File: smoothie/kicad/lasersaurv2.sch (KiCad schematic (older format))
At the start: 25 parts, among them IC1 74LV11, IC2 74HCT08, J1 DOOR1, J2 DOOR2, J3 CHILLER, J4 TO_J8, J6 TO_AUX1, J7 LASER_AUX, J8 LASER

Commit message: Fix bug where door inputs were connected before the filter.
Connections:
- net P2.11: now also C2.1, IC1.5 (2C), R7.1; no longer J2.2 (P2), R4.2, R7.2
- net P2.12: now also C3.1, IC1.4 (2B), R6.1; no longer J1.2 (P2), R3.2, R6.2
- net P4.28: now also C1.1, IC1.2 (1B), R8.1; no longer J3.2 (P2), R5.2, R8.2
- new net: J1.2 (P2), R3.2, R6.2
- new net: J2.2 (P2), R4.2, R7.2
- new net: J3.2 (P2), R5.2, R8.2
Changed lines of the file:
@@
 	1    0    0    -1
 $EndComp
-Text GLabel 3000 4250 1    60   Input ~ 0
+Text GLabel 4050 4300 1    60   Input ~ 0
 P2.11
-Text GLabel 3150 4250 1    60   Input ~ 0
+Text GLabel 4250 4300 1    60   Input ~ 0
 P2.12
-Text GLabel 3600 2700 1    60   Input ~ 0
+Text GLabel 4100 2700 1    60   Input ~ 0
 P4.28
 $Comp
@@
 Wire Wire Line
 	2650 4650 3650 4650
-Connection ~ 3000 4650
-Connection ~ 3150 4550
 Wire Wire Line
 	4950 3450 5500 3450
@@
 Wire Wire Line
 	3150 2950 3700 2950
-Wire Wire Line
-	3600 2900 3600 3000
 Connection ~ 3600 2950
 $Comp
@@
 	2400 5350 2400 5150
 Wire Wire Line
-	3150 4250 3150 4550
-Wire Wire Line
-	3000 4250 3000 4650
-Wire Wire Line
 	2650 5350 2650 4650
 Connection ~ 2400 5350
@@
 	3600 3300 3600 3400
 Wire Wire Line
-	3600 2950 3600 2700
-Wire Wire Line
 	3600 3350 4100 3350
 Wire Wire Line
@@
 	4950 2950 4950 3450
 Wire Wire Line
-	4100 2950 4100 3000
+	4100 2700 4100 3000
 Connection ~ 4100 2950
 $Comp
@@
 Wire Wire Line
 	2250 1150 2250 1000
+Wire Wire Line
+	3600 2950 3600 3000
+Wire Wire Line
+	4050 4300 4050 4650
+Connection ~ 4050 4650
+Wire Wire Line
+	4250 4300 4250 4550
+Connection ~ 4250 4550
 $EndSCHEMATC

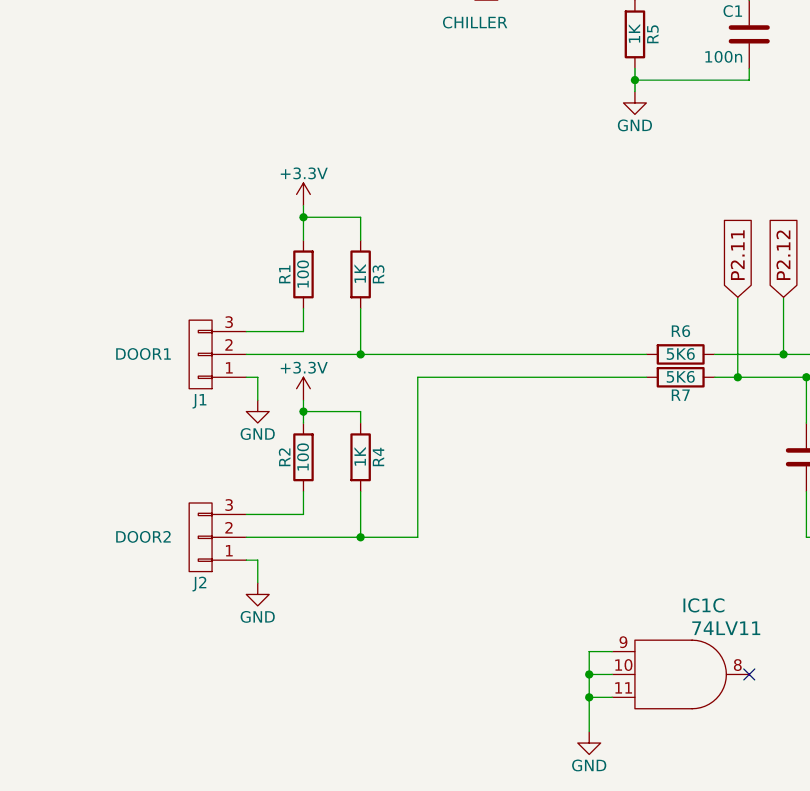
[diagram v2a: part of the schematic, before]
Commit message: Fix door switch high/low.
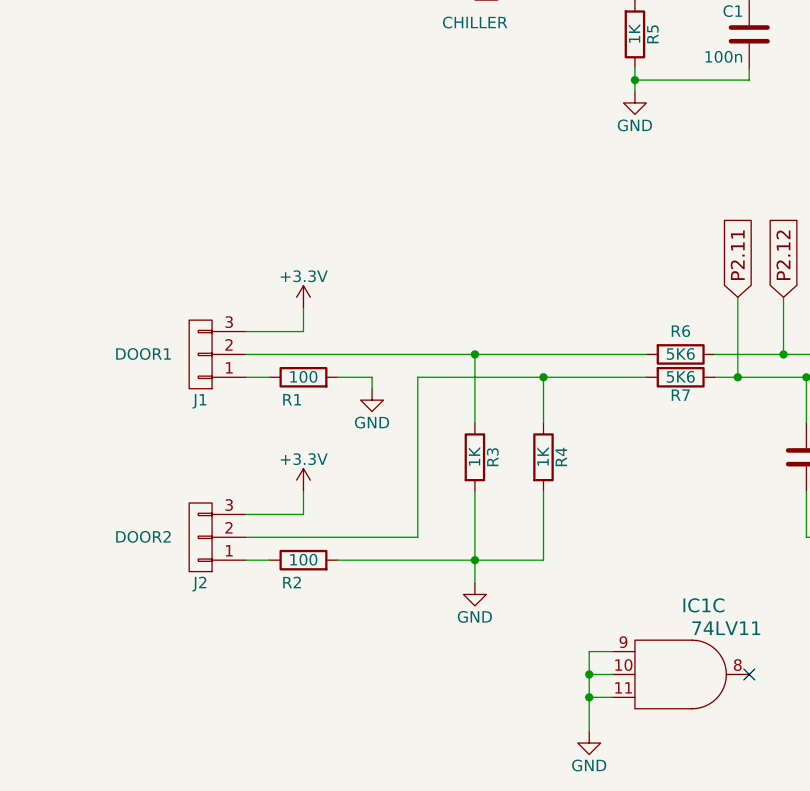
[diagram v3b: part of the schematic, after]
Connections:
- net +3V3: now also J1.3 (P3), J2.3 (P3); no longer R1.2, R2.2, R3.1, R4.1
- net GND: now also R1.2, R2.2, R3.2, R4.2; no longer J1.1 (P1), J2.1 (P1)
- net at J1.2 (P2), R6.2: now also R3.1; no longer R3.2
- net at J2.2 (P2), R7.2: now also R4.1; no longer R4.2
- net at R1.1: now also J1.1 (P1); no longer J1.3 (P3)
- net at R2.1: now also J2.1 (P1); no longer J2.3 (P3)
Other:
- moved on the sheet: R1, R2, R3, R4
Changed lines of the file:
@@
 L R R3
 U 1 1 58F2E564
-P 2400 4200
-F 0 "R3" V 2480 4200 50  0000 C CNN
-F 1 "1K" V 2400 4200 50  0000 C CNN
-F 2 "Resistors_SMD:R_0603" V 2330 4200 50  0001 C CNN
-F 3 "" H 2400 4200 50  0000 C CNN
-	1    2400 4200
+P 2900 5000
+F 0 "R3" V 2980 5000 50  0000 C CNN
+F 1 "1K" V 2900 5000 50  0000 C CNN
+F 2 "Resistors_SMD:R_0603" V 2830 5000 50  0001 C CNN
+F 3 "" H 2900 5000 50  0000 C CNN
+	1    2900 5000
 	1    0    0    -1
 $EndComp
@@
 L R R4
 U 1 1 58F2E56B
-P 2400 5000
-F 0 "R4" V 2480 5000 50  0000 C CNN
-F 1 "1K" V 2400 5000 50  0000 C CNN
-F 2 "Resistors_SMD:R_0603" V 2330 5000 50  0001 C CNN
-F 3 "" H 2400 5000 50  0000 C CNN
-	1    2400 5000
+P 3200 5000
+F 0 "R4" V 3280 5000 50  0000 C CNN
+F 1 "1K" V 3200 5000 50  0000 C CNN
+F 2 "Resistors_SMD:R_0603" V 3130 5000 50  0001 C CNN
+F 3 "" H 3200 5000 50  0000 C CNN
+	1    3200 5000
 	1    0    0    -1
 $EndComp
@@
 L R R1
 U 1 1 58F2E6E6
-P 2150 4200
-F 0 "R1" V 2230 4200 50  0000 C CNN
-F 1 "100" V 2150 4200 50  0000 C CNN
-F 2 "Resistors_SMD:R_0603" V 2080 4200 50  0001 C CNN
-F 3 "" H 2150 4200 50  0000 C CNN
-	1    2150 4200
-	-1   0    0    1
+P 2150 4650
+F 0 "R1" V 2050 4700 50  0000 C CNN
+F 1 "100" V 2150 4650 50  0000 C CNN
+F 2 "Resistors_SMD:R_0603" V 2080 4650 50  0001 C CNN
+F 3 "" H 2150 4650 50  0000 C CNN
+	1    2150 4650
+	0    -1   -1   0
 $EndComp
 $Comp
 L GND #PWR010
 U 1 1 58F2E6ED
-P 1950 4750
-F 0 "#PWR010" H 1950 4500 50  0001 C CNN
-F 1 "GND" H 1950 4600 50  0000 C CNN
-F 2 "" H 1950 4750 50  0000 C CNN
-F 3 "" H 1950 4750 50  0000 C CNN
-	1    1950 4750
+P 2450 4700
+F 0 "#PWR010" H 2450 4450 50  0001 C CNN
+F 1 "GND" H 2450 4550 50  0000 C CNN
+F 2 "" H 2450 4700 50  0000 C CNN
+F 3 "" H 2450 4700 50  0000 C CNN
+	1    2450 4700
 	1    0    0    -1
 $EndComp
@@
 L R R2
 U 1 1 58F2E700
-P 2150 5000
-F 0 "R2" V 2230 5000 50  0000 C CNN
-F 1 "100" V 2150 5000 50  0000 C CNN
-F 2 "Resistors_SMD:R_0603" V 2080 5000 50  0001 C CNN
-F 3 "" H 2150 5000 50  0000 C CNN
-	1    2150 5000
-	-1   0    0    1
+P 2150 5450
+F 0 "R2" V 2050 5500 50  0000 C CNN
+F 1 "100" V 2150 5450 50  0000 C CNN
+F 2 "Resistors_SMD:R_0603" V 2080 5450 50  0001 C CNN
+F 3 "" H 2150 5450 50  0000 C CNN
+	1    2150 5450
+	0    -1   -1   0
 $EndComp
 $Comp
 L GND #PWR011
 U 1 1 58F2E707
-P 1950 5550
-F 0 "#PWR011" H 1950 5300 50  0001 C CNN
-F 1 "GND" H 1950 5400 50  0000 C CNN
-F 2 "" H 1950 5550 50  0000 C CNN
-F 3 "" H 1950 5550 50  0000 C CNN
-	1    1950 5550
+P 2900 5550
+F 0 "#PWR011" H 2900 5300 50  0001 C CNN
+F 1 "GND" H 2900 5400 50  0000 C CNN
+F 2 "" H 2900 5550 50  0000 C CNN
+F 3 "" H 2900 5550 50  0000 C CNN
+	1    2900 5550
 	1    0    0    -1
 $EndComp
@@
 	1900 4550 3650 4550
 Wire Wire Line
-	2400 4550 2400 4350
-Connection ~ 2400 4550
-Wire Wire Line
-	1900 4650 1950 4650
-Wire Wire Line
-	1950 4650 1950 4750
+	1900 4650 2000 4650
 Wire Wire Line
 	2150 5150 2150 5250
@@
 	1900 5350 2650 5350
 Wire Wire Line
-	2400 5350 2400 5150
-Wire Wire Line
 	2650 5350 2650 4650
-Connection ~ 2400 5350
-Wire Wire Line
-	1900 5450 1950 5450
-Wire Wire Line
-	1950 5450 1950 5550
 $Comp
 L +3.3V #PWR016
 U 1 1 58F316F9
-P 2150 3900
-F 0 "#PWR016" H 2150 3750 50  0001 C CNN
-F 1 "+3.3V" H 2150 4040 50  0000 C CNN
-F 2 "" H 2150 3900 50  0001 C CNN
-F 3 "" H 2150 3900 50  0001 C CNN
-	1    2150 3900
-	1    0    0    -1
-$EndComp
-Wire Wire Line
-	2150 3900 2150 4050
-Wire Wire Line
-	2400 4050 2400 3950
-Wire Wire Line
-	2400 3950 2150 3950
-Connection ~ 2150 3950
+P 2150 4350
+F 0 "#PWR016" H 2150 4200 50  0001 C CNN
+F 1 "+3.3V" H 2150 4490 50  0000 C CNN
+F 2 "" H 2150 4350 50  0001 C CNN
+F 3 "" H 2150 4350 50  0001 C CNN
+	1    2150 4350
+	1    0    0    -1
+$EndComp
 $Comp
 L +3.3V #PWR017
 U 1 1 58F318DD
-P 2150 4750
-F 0 "#PWR017" H 2150 4600 50  0001 C CNN
-F 1 "+3.3V" H 2150 4890 50  0000 C CNN
-F 2 "" H 2150 4750 50  0001 C CNN
-F 3 "" H 2150 4750 50  0001 C CNN
-	1    2150 4750
-	1    0    0    -1
-$EndComp
-Wire Wire Line
-	2150 4750 2150 4850
-Wire Wire Line
-	2150 4800 2400 4800
-Wire Wire Line
-	2400 4800 2400 4850
-Connection ~ 2150 4800
+P 2150 5150
+F 0 "#PWR017" H 2150 5000 50  0001 C CNN
+F 1 "+3.3V" H 2150 5290 50  0000 C CNN
+F 2 "" H 2150 5150 50  0001 C CNN
+F 3 "" H 2150 5150 50  0001 C CNN
+	1    2150 5150
+	1    0    0    -1
+$EndComp
 Text GLabel 4650 4300 1    60   Input ~ 0
 P1.22
@@
 	4250 4300 4250 4550
 Connection ~ 4250 4550
+Wire Wire Line
+	2900 4850 2900 4550
+Connection ~ 2900 4550
+Wire Wire Line
+	3200 4650 3200 4850
+Connection ~ 3200 4650
+Wire Wire Line
+	3200 5450 3200 5150
+Wire Wire Line
+	2900 5150 2900 5550
+Connection ~ 2900 5450
+Wire Wire Line
+	1900 5450 2000 5450
+Wire Wire Line
+	2300 5450 3200 5450
+Wire Wire Line
+	2300 4650 2450 4650
+Wire Wire Line
+	2450 4650 2450 4700
 $EndSCHEMATC
